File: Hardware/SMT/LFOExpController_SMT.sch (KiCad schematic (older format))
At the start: 54 parts

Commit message: correction
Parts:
- removed C_BP2, C_BP4: 100nF, Capacitors_SMD:C_0805_HandSoldering, symbol C
- removed C_BP3: 1uF, Capacitors_SMD:C_0805_HandSoldering, symbol C
- removed R_OA_FB1: 10K, Resistors_SMD:R_0805_HandSoldering, symbol R
- removed R_OA_GAIN1: 5K6, Resistors_SMD:R_0805_HandSoldering, symbol R
- removed R_OA_GAIN2: 12K, Resistors_SMD:R_0805_HandSoldering, symbol R
- removed SW_OAGAIN1: SW_SPDT, C&K_8_6mm_SPDT_ONON:C&K_8_6mm_SPDT_ONON, symbol SW_SPDT
- removed U_OUT_DAC1: MCP4921, Housings_SOIC:SOIC-8_3.9x4.9mm_Pitch1.27mm, symbol MCP4921
- removed U_OUT_OA1: MCP601-xSN, Housings_SOIC:SOIC-8_3.9x4.9mm_Pitch1.27mm, symbol MCP601-xSN
- added U_DIGPOT1: MCP41050, symbol MCP41050
- R_FUNC1: value 10K -> 1K
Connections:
- net +5V: now also U_DIGPOT1.8 (VDD); no longer J_OUT1.2
- net DACCS: now also U_DIGPOT1.1 (~CS)
- net GND: now also U_DIGPOT1.4 (VSS); no longer J_OUT1.3
- net MOSI: now also U_DIGPOT1.3 (SI)
- net SCK: now also U_DIGPOT1.2 (SCK)
- net SW_FUNC: now also U_AVR1.9 ((PCINT21/OC0B/T1)PD5); no longer U_AVR1.30 ((PCINT16/RXD)PD0)
- net OA_SWEN: no longer names the net of SW_EN1.5 (B)
- net OA_SWEN: now also U_DIGPOT1.6 (PW0)
- net SWEN_OUT renamed TIP_SIGOUT
- new net RING_SIGOUT: J_OUT1.2, U_DIGPOT1.7 (PB0)
- new net SLEEVE_SIGOUT: J_OUT1.3, U_DIGPOT1.5 (PA0)
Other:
- note added: "ONLY USED FOR ISP"
- note removed: "Selects either 5V(default) or 3V3 output"
- moved on the sheet: C_AVRCLK1, C_AVRCLK2, C_BP5, C_DB1, J_AUX2MAIN1, J_ISP1, J_MAIN2AUX1, J_OUT1, R_DB1, R_FREQ1, R_FUNC1, R_MUXIN1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

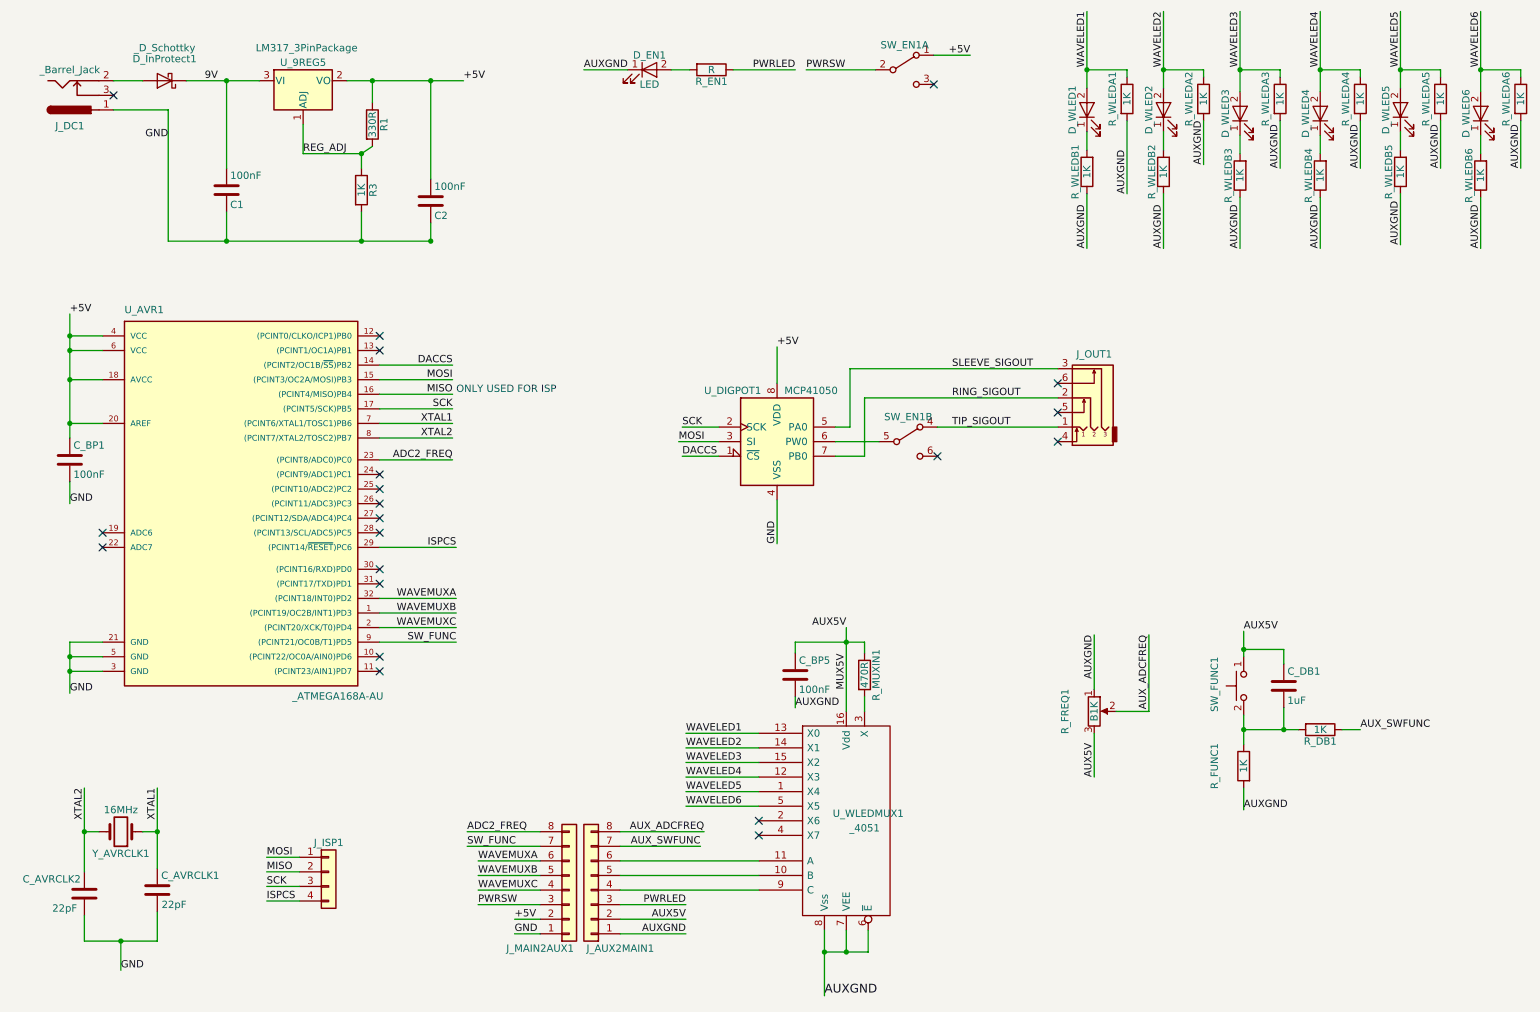
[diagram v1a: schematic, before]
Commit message: Completed Board Layout
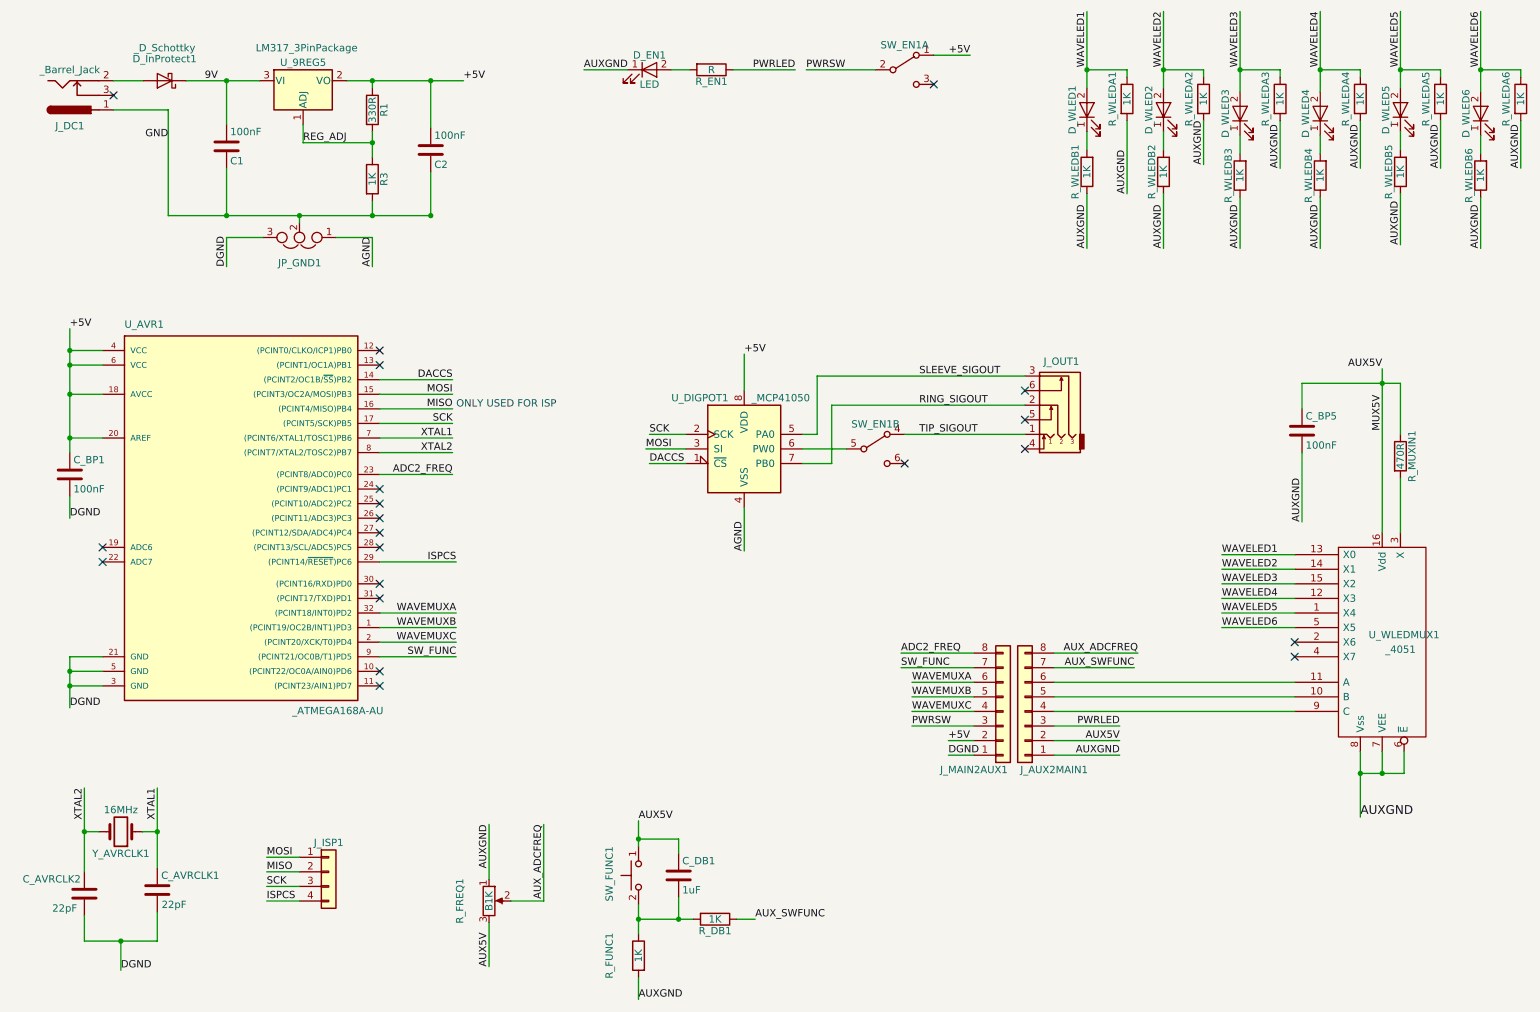
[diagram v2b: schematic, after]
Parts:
- removed J_AUX2MAIN1: Conn_01x08, Pin_Headers:Pin_Header_Straight_1x08_Pitch2.54mm, symbol Conn_01x08
- removed U_DIGPOT1: MCP41050, symbol MCP41050
- added JP_GND1: Jumper_NC_Dual, NetTie-II_SMD_FakeConnected:NetTie-II_SMD_GraphicallyConnected, symbol Jumper_NC_Dual
- added J_AUX2MAIN1: _Conn_01x08, Pin_Headers:Pin_Header_Straight_1x08_Pitch2.54mm, symbol _Conn_01x08
- added U_DIGPOT1: _MCP41050, Housings_SOIC:SOIC-8_3.9x4.9mm_Pitch1.27mm, symbol _MCP41050
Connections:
- net +5V: now also U_DIGPOT1.8 (VDD)
- net AUX5V: now also J_AUX2MAIN1.2 (Pin_2)
- net AUXGND: now also J_AUX2MAIN1.1 (Pin_1)
- net AUX_ADCFREQ: now also J_AUX2MAIN1.8 (Pin_8)
- net AUX_SWFUNC: now also J_AUX2MAIN1.7 (Pin_7)
- net DACCS: now also U_DIGPOT1.1 (~CS)
- net GND: now also JP_GND1.2; no longer C_AVRCLK1.1, C_AVRCLK2.1, C_BP1.2, J_MAIN2AUX1.1 (Pin_1), U_AVR1.21 (GND), U_AVR1.3 (GND), U_AVR1.5 (GND)
- net MOSI: now also U_DIGPOT1.3 (SI)
- net PWRLED: now also J_AUX2MAIN1.3 (Pin_3)
- net RING_SIGOUT: now also U_DIGPOT1.7 (PB0)
- net SCK: now also U_DIGPOT1.2 (SCK)
- net SLEEVE_SIGOUT: now also U_DIGPOT1.5 (PA0)
- net at SW_EN1.5 (B): now also U_DIGPOT1.6 (PW0)
- net at U_WLEDMUX1.10 (B): now also J_AUX2MAIN1.5 (Pin_5)
- net at U_WLEDMUX1.11 (A): now also J_AUX2MAIN1.6 (Pin_6)
- net at U_WLEDMUX1.9 (C): now also J_AUX2MAIN1.4 (Pin_4)
- new net AGND: JP_GND1.1, U_DIGPOT1.4 (VSS)
- new net DGND: C_AVRCLK1.1, C_AVRCLK2.1, C_BP1.2, JP_GND1.3, J_MAIN2AUX1.1 (Pin_1), U_AVR1.21 (GND), U_AVR1.3 (GND), U_AVR1.5 (GND)
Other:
- moved on the sheet: C1, C2, C_BP1, C_BP5, C_DB1, J_MAIN2AUX1, J_OUT1, R1, R3, R_DB1, R_FREQ1, R_FUNC1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

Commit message: Revision3 update
- Added ground to Jack sleeve pin
- Corrected SW_FUNC circuit
- Removed R_WLEDB LEDS
- Modified firmware from eight wavepatterns to six, to allign with Hardware (Sine, Triangle, RampUp, Step4, Square, Pulse)
- Created R3 documentation
- Created new GERBERS
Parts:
- removed R_WLEDB1, R_WLEDB2, R_WLEDB3, R_WLEDB4, R_WLEDB5, R_WLEDB6: 1K, Resistors_SMD:R_0805_HandSoldering, symbol R
- R_EN1: value R -> 1K
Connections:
- net SLEEVE_SIGOUT is gone; now on net AGND: J_OUT1.3, U_DIGPOT1.5 (PA0)
- net AUXGND: now also D_WLED1.1 (K), D_WLED2.1 (K), D_WLED3.1 (K), D_WLED4.1 (K), D_WLED5.1 (K), D_WLED6.1 (K)
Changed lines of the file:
@@
 encoding utf-8
 Sheet 1 1
-Title ""
-Date ""
-Rev ""
+Title "LFO Expression Controller Pedal"
+Date "2018-03-24"
+Rev "3"
 Comp ""
 Comment1 ""
-Comment2 "Ouput is aliased using 12bit DAC and amplified to 5VDC using MCP601 opamp"
-Comment3 "Uses ATMEGA328P MCU to generate WaveForms"
-Comment4 "LFO Controller Pedal"
+Comment2 "Design by Chris Sutton"
+Comment3 "https://github.com/cracked-machine/LFOExpressionControllerPedal"
+Comment4 "Uses ATMEGA328P MCU to control digital potentiometer"
 $EndDescr
 $Comp
@@
 	0    -1   -1   0
 $EndComp
-$Comp
-L R R_WLEDB1
-U 1 1 5A9EB170
-P 8025 1850
-F 0 "R_WLEDB1" V 8105 1850 50  0000 C CNN
-F 1 "1K" V 8025 1850 50  0000 C CNN
-F 2 "Resistors_SMD:R_0805_HandSoldering" V 7955 1850 50  0001 C CNN
-F 3 "" H 8025 1850 50  0001 C CNN
-	1    8025 1850
-	-1   0    0    1
-$EndComp
 Text Label 8025 2375 1    50   ~ 0
 AUXGND
@@
 P 5450 1150
 F 0 "R_EN1" V 5530 1150 50  0000 C CNN
-F 1 "R" V 5450 1150 50  0000 C CNN
+F 1 "1K" V 5450 1150 50  0000 C CNN
 F 2 "Resistors_SMD:R_0805_HandSoldering" V 5380 1150 50  0001 C CNN
 F 3 "" H 5450 1150 50  0001 C CNN
@@
 	0    -1   -1   0
 $EndComp
-$Comp
-L R R_WLEDB2
-U 1 1 5AA1B322
-P 8550 1850
-F 0 "R_WLEDB2" V 8630 1850 50  0000 C CNN
-F 1 "1K" V 8550 1850 50  0000 C CNN
-F 2 "Resistors_SMD:R_0805_HandSoldering" V 8480 1850 50  0001 C CNN
-F 3 "" H 8550 1850 50  0001 C CNN
-	1    8550 1850
-	-1   0    0    1
-$EndComp
 Text Label 8550 2375 1    50   ~ 0
 AUXGND
@@
 	0    -1   -1   0
 $EndComp
-$Comp
-L R R_WLEDB3
-U 1 1 5AA1B982
-P 9075 1875
-F 0 "R_WLEDB3" V 9155 1875 50  0000 C CNN
-F 1 "1K" V 9075 1875 50  0000 C CNN
-F 2 "Resistors_SMD:R_0805_HandSoldering" V 9005 1875 50  0001 C CNN
-F 3 "" H 9075 1875 50  0001 C CNN
-	1    9075 1875
-	-1   0    0    1
-$EndComp
 Text Label 9075 2375 1    50   ~ 0
 AUXGND
@@
 	0    -1   -1   0
 $EndComp
-$Comp
-L R R_WLEDB4
-U 1 1 5AA1BA9B
-P 9625 1875
-F 0 "R_WLEDB4" V 9705 1875 50  0000 C CNN
-F 1 "1K" V 9625 1875 50  0000 C CNN
-F 2 "Resistors_SMD:R_0805_HandSoldering" V 9555 1875 50  0001 C CNN
-F 3 "" H 9625 1875 50  0001 C CNN
-	1    9625 1875
-	-1   0    0    1
-$EndComp
 Text Label 9625 2375 1    50   ~ 0
 AUXGND
@@
 	0    -1   -1   0
 $EndComp
-$Comp
-L R R_WLEDB5
-U 1 1 5AA1BBB4
-P 10175 1850
-F 0 "R_WLEDB5" V 10255 1850 50  0000 C CNN
-F 1 "1K" V 10175 1850 50  0000 C CNN
-F 2 "Resistors_SMD:R_0805_HandSoldering" V 10105 1850 50  0001 C CNN
-F 3 "" H 10175 1850 50  0001 C CNN
-	1    10175 1850
-	-1   0    0    1
-$EndComp
 Text Label 10175 2350 1    50   ~ 0
 AUXGND
@@
 	0    -1   -1   0
 $EndComp
-$Comp
-L R R_WLEDB6
-U 1 1 5AA1BCF1
-P 10725 1875
-F 0 "R_WLEDB6" V 10805 1875 50  0000 C CNN
-F 1 "1K" V 10725 1875 50  0000 C CNN
-F 2 "Resistors_SMD:R_0805_HandSoldering" V 10655 1875 50  0001 C CNN
-F 3 "" H 10725 1875 50  0001 C CNN
-	1    10725 1875
-	-1   0    0    1
-$EndComp
 Text Label 10725 2375 1    50   ~ 0
 AUXGND
@@
 Connection ~ 2125 1225
 Wire Wire Line
-	5625 6975 5750 6975
-Wire Wire Line
 	7250 5350 6825 5350
 Wire Wire Line
@@
 	8025 750  8025 1275
 Wire Wire Line
-	8025 1575 8025 1700
-Wire Wire Line
-	8025 2000 8025 2375
-Wire Wire Line
-	7600 3250 6175 3250
+	8025 1575 8025 2375
+Wire Wire Line
+	6175 3250 7600 3250
 Wire Wire Line
 	1050 3375 1275 3375
@@
 	8550 750  8550 1275
 Wire Wire Line
-	8550 1575 8550 1700
-Wire Wire Line
-	8550 2000 8550 2375
+	8550 1575 8550 2375
 Wire Wire Line
 	8825 1200 8825 1150
@@
 	9075 750  9075 1300
 Wire Wire Line
-	9075 1600 9075 1725
-Wire Wire Line
-	9075 2025 9075 2375
+	9075 1600 9075 2375
 Wire Wire Line
 	9350 1200 9350 1150
@@
 	9625 750  9625 1300
 Wire Wire Line
-	9625 1600 9625 1725
-Wire Wire Line
-	9625 2025 9625 2375
+	9625 1600 9625 2375
 Wire Wire Line
 	9900 1200 9900 1150
@@
 	10175 750  10175 1275
 Wire Wire Line
-	10175 1575 10175 1700
-Wire Wire Line
-	10175 2000 10175 2350
+	10175 1575 10175 2350
 Wire Wire Line
 	10450 1200 10450 1150
@@
 	10725 750  10725 1300
 Wire Wire Line
-	10725 1600 10725 1725
-Wire Wire Line
-	10725 2025 10725 2375
+	10725 1600 10725 2375
 Wire Wire Line
 	11000 1200 11000 1150
@@
 	1    0    0    -1
 $EndComp
-Wire Wire Line
-	5225 6525 5225 6425
-Wire Wire Line
-	5225 6425 4950 6425
 Connection ~ 4950 6425
 Wire Wire Line
@@
 	-1   0    0    1
 $EndComp
+Wire Wire Line
+	7475 3250 7475 2900
+Connection ~ 7475 3250
+Text Label 7475 2900 3    50   ~ 0
+AGND
+Wire Wire Line
+	5625 6975 5750 6975
+Wire Wire Line
+	4950 6425 5225 6425
+Wire Wire Line
+	5225 6425 5225 6525
 $EndSCHEMATC
